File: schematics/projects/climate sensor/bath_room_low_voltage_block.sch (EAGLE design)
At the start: 18 parts, among them Q1 KT3102BM, Q2 KT3102BM, Q3 KT3102BM, Q4 KT3102BM, Q5 KT3102BM

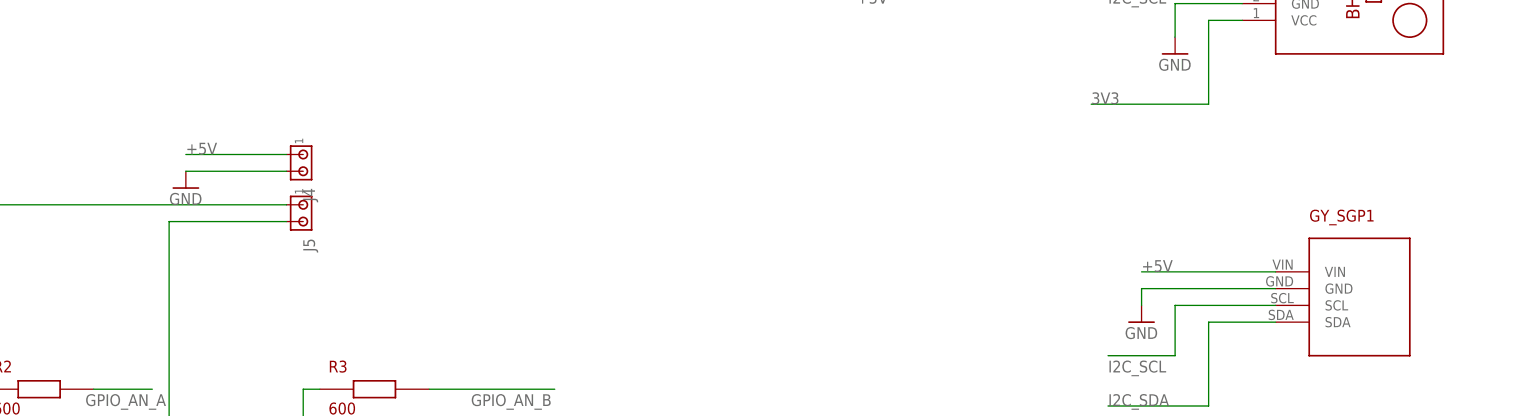
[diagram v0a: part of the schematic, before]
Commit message: added eagle board files for low-voltage schemas
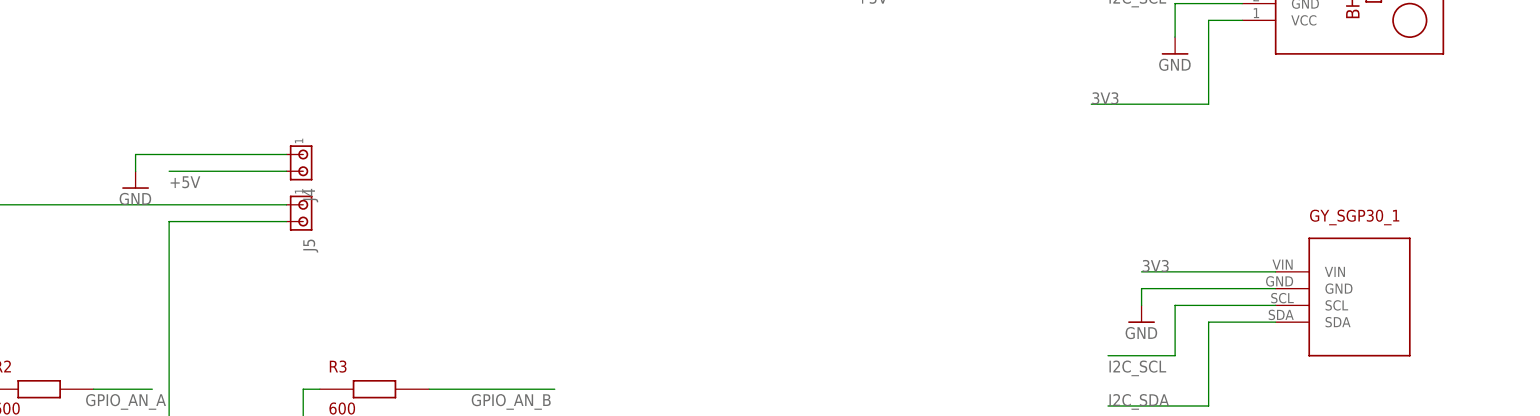
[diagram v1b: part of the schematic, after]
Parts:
- renumbered GY_SGP1 to GY_SGP30_1
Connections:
- net +5V: now also J4.2; no longer GY_SGP30_1.VIN, J4.1
- net 3V3: now also GY_SGP30_1.VIN
- net GND: now also J4.1; no longer J4.2
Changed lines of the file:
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@@
 <schematic_group name="RGBLED1"/>
 <schematic_group name="BH1"/>
-<schematic_group name="GY-SGP1"/>
+<schematic_group name="GY_SGP30"/>
 <schematic_group name="5V_SUPPLY_JET1"/>
 <schematic_group name="ANEMOMETER1"/>
@@
 <part name="GND5" library="supply1" library_urn="urn:adsk.eagle:library:371" deviceset="GND" device=""/>
 <part name="GND6" library="supply1" library_urn="urn:adsk.eagle:library:371" deviceset="GND" device=""/>
-<part name="GY_SGP1" library="my_devices" deviceset="GY-SGP30" device=""/>
+<part name="GY_SGP30_1" library="my_devices" deviceset="GY-SGP30" device=""/>
 <part name="J2" library="con-amp" library_urn="urn:adsk.eagle:library:127" deviceset="MTA02-100" device="" package3d_urn="urn:adsk.eagle:package:8081649/1"/>
 <part name="C1" library="my_devices" deviceset="C" device="" value="1000 mF"/>
@@
 <part name="J4" library="con-amp" library_urn="urn:adsk.eagle:library:127" deviceset="MTA02-100" device="" package3d_urn="urn:adsk.eagle:package:8081649/1"/>
 <part name="J5" library="con-amp" library_urn="urn:adsk.eagle:library:127" deviceset="MTA02-100" device="" package3d_urn="urn:adsk.eagle:package:8081649/1"/>
-<part name="GND10" library="supply1" library_urn="urn:adsk.eagle:library:371" deviceset="GND" device=""/>
 <part name="Q4" library="my_devices" deviceset="TRANSISTOR_NPN" device="" value="KT3102BM"/>
 <part name="Q5" library="my_devices" deviceset="TRANSISTOR_NPN" device="" value="KT3102BM"/>
 <part name="R2" library="my_devices" deviceset="R" device="" value="600"/>
 <part name="R3" library="my_devices" deviceset="R" device="" value="600"/>
+<part name="GND1" library="supply1" library_urn="urn:adsk.eagle:library:371" deviceset="GND" device=""/>
 </parts>
 <sheets>
@@
 <attribute name="VALUE" x="81.28" y="2.54" size="1.778" layer="96"/>
 </instance>
-<instance part="GND6" gate="1" x="78.74" y="-35.56" smashed="yes" grouprefs="GY-SGP1">
+<instance part="GND6" gate="1" x="78.74" y="-35.56" smashed="yes" grouprefs="GY_SGP30">
 <attribute name="VALUE" x="76.2" y="-38.1" size="1.778" layer="96"/>
 </instance>
-<instance part="GY_SGP1" gate="G$1" x="106.68" y="-30.48" smashed="yes" grouprefs="GY-SGP1">
+<instance part="GY_SGP30_1" gate="G$1" x="106.68" y="-30.48" smashed="yes" grouprefs="GY_SGP30">
 <attribute name="NAME" x="104.14" y="-20.32" size="1.778" layer="94"/>
 </instance>
@@
 <attribute name="VALUE" x="-52.07" y="-22.86" size="1.778" layer="96" rot="R270"/>
 </instance>
-<instance part="GND10" gate="1" x="-66.04" y="-15.24" smashed="yes" grouprefs="ANEMOMETER1">
-<attribute name="VALUE" x="-68.58" y="-17.78" size="1.778" layer="96"/>
-</instance>
 <instance part="Q4" gate="G$1" x="-48.26" y="-68.58" smashed="yes" grouprefs="ANEMOMETER1">
 <attribute name="NAME" x="-40.64" y="-66.04" size="1.778" layer="94"/>
@@
 <attribute name="NAME" x="-44.45" y="-43.18" size="1.778" layer="94"/>
 <attribute name="VALUE" x="-44.45" y="-49.53" size="1.778" layer="94"/>
+</instance>
+<instance part="GND1" gate="1" x="-73.66" y="-15.24" smashed="yes">
+<attribute name="VALUE" x="-76.2" y="-17.78" size="1.778" layer="96"/>
 </instance>
 </instances>
@@
 </segment>
 <segment>
-<wire x1="99.06" y1="-30.48" x2="78.74" y2="-30.48" width="0.1524" layer="91" grouprefs="GY-SGP1"/>
+<wire x1="99.06" y1="-30.48" x2="78.74" y2="-30.48" width="0.1524" layer="91" grouprefs="GY_SGP30"/>
 <pinref part="GND6" gate="1" pin="GND"/>
-<wire x1="78.74" y1="-30.48" x2="78.74" y2="-33.02" width="0.1524" layer="91" grouprefs="GY-SGP1"/>
-<pinref part="GY_SGP1" gate="G$1" pin="GND"/>
+<wire x1="78.74" y1="-30.48" x2="78.74" y2="-33.02" width="0.1524" layer="91" grouprefs="GY_SGP30"/>
+<pinref part="GY_SGP30_1" gate="G$1" pin="GND"/>
 </segment>
 <segment>
@@
 </segment>
 <segment>
-<pinref part="GND10" gate="1" pin="GND"/>
-<pinref part="J4" gate="G$1" pin="2"/>
-<wire x1="-66.04" y1="-12.7" x2="-50.8" y2="-12.7" width="0.1524" layer="91" grouprefs="ANEMOMETER1"/>
+<pinref part="J4" gate="G$1" pin="1"/>
+<wire x1="-50.8" y1="-10.16" x2="-73.66" y2="-10.16" width="0.1524" layer="91"/>
+<wire x1="-73.66" y1="-10.16" x2="-73.66" y2="-12.7" width="0.1524" layer="91"/>
+<pinref part="GND1" gate="1" pin="GND"/>
 </segment>
 </net>
@@
 </segment>
 <segment>
-<wire x1="99.06" y1="-33.02" x2="83.82" y2="-33.02" width="0.1524" layer="91" grouprefs="GY-SGP1"/>
-<wire x1="83.82" y1="-33.02" x2="83.82" y2="-40.64" width="0.1524" layer="91" grouprefs="GY-SGP1"/>
-<wire x1="83.82" y1="-40.64" x2="73.66" y2="-40.64" width="0.1524" layer="91" grouprefs="GY-SGP1"/>
-<label x="73.66" y="-43.18" size="1.778" layer="95" grouprefs="GY-SGP1"/>
-<pinref part="GY_SGP1" gate="G$1" pin="SCL"/>
+<wire x1="99.06" y1="-33.02" x2="83.82" y2="-33.02" width="0.1524" layer="91" grouprefs="GY_SGP30"/>
+<wire x1="83.82" y1="-33.02" x2="83.82" y2="-40.64" width="0.1524" layer="91" grouprefs="GY_SGP30"/>
+<wire x1="83.82" y1="-40.64" x2="73.66" y2="-40.64" width="0.1524" layer="91" grouprefs="GY_SGP30"/>
+<label x="73.66" y="-43.18" size="1.778" layer="95" grouprefs="GY_SGP30"/>
+<pinref part="GY_SGP30_1" gate="G$1" pin="SCL"/>
 </segment>
 </net>
@@
 </segment>
 <segment>
-<wire x1="99.06" y1="-35.56" x2="88.9" y2="-35.56" width="0.1524" layer="91" grouprefs="GY-SGP1"/>
-<wire x1="88.9" y1="-35.56" x2="88.9" y2="-48.26" width="0.1524" layer="91" grouprefs="GY-SGP1"/>
-<wire x1="88.9" y1="-48.26" x2="73.66" y2="-48.26" width="0.1524" layer="91" grouprefs="GY-SGP1"/>
-<label x="73.66" y="-48.26" size="1.778" layer="95" grouprefs="GY-SGP1"/>
-<pinref part="GY_SGP1" gate="G$1" pin="SDA"/>
+<wire x1="99.06" y1="-35.56" x2="88.9" y2="-35.56" width="0.1524" layer="91" grouprefs="GY_SGP30"/>
+<wire x1="88.9" y1="-35.56" x2="88.9" y2="-48.26" width="0.1524" layer="91" grouprefs="GY_SGP30"/>
+<wire x1="88.9" y1="-48.26" x2="73.66" y2="-48.26" width="0.1524" layer="91" grouprefs="GY_SGP30"/>
+<label x="73.66" y="-48.26" size="1.778" layer="95" grouprefs="GY_SGP30"/>
+<pinref part="GY_SGP30_1" gate="G$1" pin="SDA"/>
 </segment>
 </net>
@@
 <wire x1="7.62" y1="48.26" x2="40.64" y2="48.26" width="0.1524" layer="91" grouprefs="ESP2"/>
 <label x="7.62" y="48.26" size="1.778" layer="95" grouprefs="ESP2"/>
-</segment>
-<segment>
-<wire x1="99.06" y1="-27.94" x2="78.74" y2="-27.94" width="0.1524" layer="91" grouprefs="GY-SGP1"/>
-<label x="78.74" y="-27.94" size="1.778" layer="95" grouprefs="GY-SGP1"/>
-<pinref part="GY_SGP1" gate="G$1" pin="VIN"/>
 </segment>
 <segment>
@@
 </segment>
 <segment>
-<pinref part="J4" gate="G$1" pin="1"/>
-<wire x1="-50.8" y1="-10.16" x2="-66.04" y2="-10.16" width="0.1524" layer="91" grouprefs="ANEMOMETER1"/>
-<label x="-66.04" y="-10.16" size="1.778" layer="95" grouprefs="ANEMOMETER1"/>
+<pinref part="J4" gate="G$1" pin="2"/>
+<wire x1="-50.8" y1="-12.7" x2="-68.58" y2="-12.7" width="0.1524" layer="91"/>
+<label x="-68.58" y="-15.24" size="1.778" layer="95"/>
 </segment>
 </net>
@@
 <label x="71.12" y="-2.54" size="1.778" layer="95" grouprefs="BH1"/>
 </segment>
-</net>
+<segment>
+<wire x1="99.06" y1="-27.94" x2="78.74" y2="-27.94" width="0.1524" layer="91" grouprefs="GY_SGP30"/>
+<label x="78.74" y="-27.94" size="1.778" layer="95" grouprefs="GY_SGP30"/>
+<pinref part="GY_SGP30_1" gate="G$1" pin="VIN"/>
+</segment>
+</net>
